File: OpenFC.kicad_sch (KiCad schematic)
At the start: 0 parts

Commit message: First routing
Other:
- sheet ELRS ports: added ESP8285_EN, ESP8285_RST; removed none
- sheet RP2350A ports: added ESP8285_EN, ESP8285_RST; removed none
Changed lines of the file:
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@@
+	(wire
+		(pts
+			(xy 87.63 76.2) (xy 104.14 76.2)
+		)
+		(stroke
+			(width 0)
+			(type default)
+		)
+	)
 	(wire
 		(pts
@@
 		(pts
 			(xy 87.63 97.79) (xy 104.14 97.79)
+		)
+		(stroke
+			(width 0)
+			(type default)
+		)
+	)
+	(wire
+		(pts
+			(xy 87.63 78.74) (xy 104.14 78.74)
 		)
 		(stroke
@@
 	)
 	(sheet
-		(at 64.77 80.01)
-		(size 22.86 7.62)
+		(at 64.77 72.39)
+		(size 22.86 15.24)
 		(exclude_from_sim no)
 		(in_bom yes)
@@
 		)
 		(property "Sheetname" "ELRS"
-			(at 64.77 79.2984 0)
+			(at 64.77 71.6784 0)
 			(effects
 				(font
@@
 		(pin "ELRX_TX" input
 			(at 87.63 85.09 0)
+			(effects
+				(font
+					(size 1.27 1.27)
+				)
+				(justify right)
+			)
+		)
+		(pin "ESP8285_EN" input
+			(at 87.63 78.74 0)
+			(effects
+				(font
+					(size 1.27 1.27)
+				)
+				(justify right)
+			)
+		)
+		(pin "ESP8285_RST" input
+			(at 87.63 76.2 0)
 			(effects
 				(font
@@
 			)
 		)
+		(pin "ESP8285_EN" input
+			(at 104.14 78.74 180)
+			(effects
+				(font
+					(size 1.27 1.27)
+				)
+				(justify left)
+			)
+		)
+		(pin "ESP8285_RST" input
+			(at 104.14 76.2 180)
+			(effects
+				(font
+					(size 1.27 1.27)
+				)
+				(justify left)
+			)
+		)

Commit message: almost finished routing
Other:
- sheet ELRS ports: added ESP_BOOT0; removed ESP8285_RST
- sheet RP2350A ports: added ESP_BOOT0; removed ESP8285_RST
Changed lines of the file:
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@@
 			)
 		)
-		(pin "ESP8285_RST" input
+		(pin "ESP_BOOT0" input
 			(at 87.63 76.2 0)
 			(effects
@@
 			)
 		)
-		(pin "ESP8285_RST" input
+		(pin "ESP_BOOT0" input
 			(at 104.14 76.2 180)
 			(effects

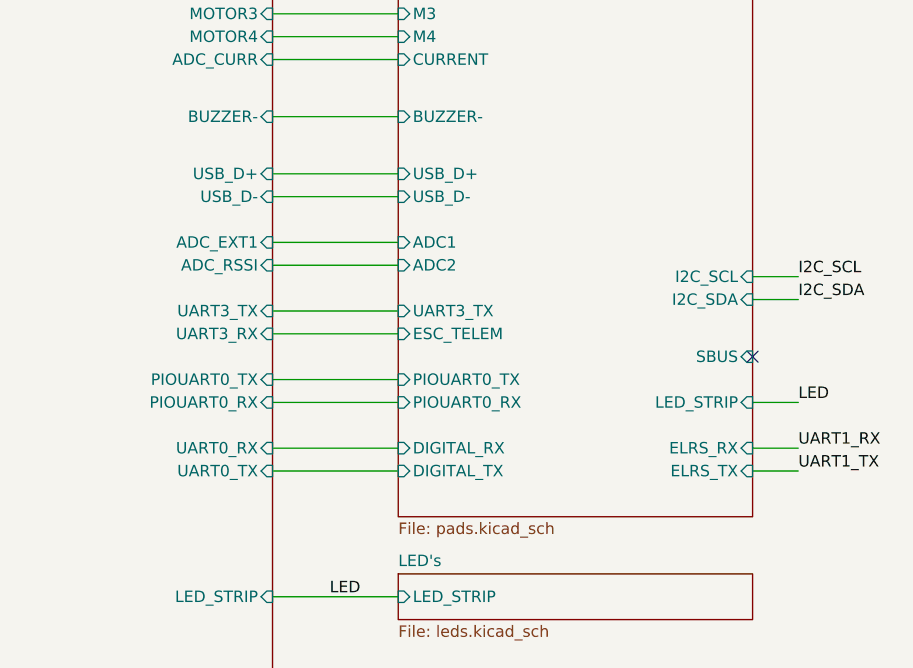
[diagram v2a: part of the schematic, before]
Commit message: Switched to RP2354A and re-routed
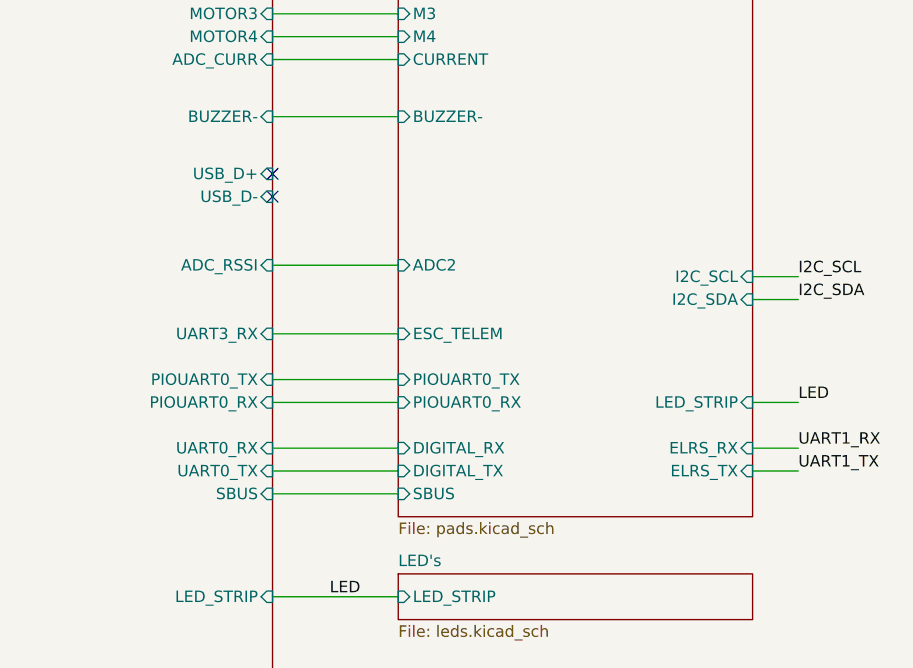
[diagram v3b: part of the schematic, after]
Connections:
- no-connect marks 1 -> 2
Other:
- sheet PADS ports: added none; removed ADC1, UART3_TX, USB_D+, USB_D-
- sheet RP2350A ports: added SBUS; removed ADC_EXT1, UART3_TX
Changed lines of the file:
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@@
 	)
 	(no_connect
-		(at 219.71 118.11)
+		(at 166.37 100.33)
+	)
+	(no_connect
+		(at 166.37 97.79)
 	)
 	(wire
@@
 		)
 	)
-	(wire
-		(pts
-			(xy 166.37 105.41) (xy 180.34 105.41)
-		)
-		(stroke
-			(width 0)
-			(type default)
-		)
-	)
 	(bus
 		(pts
@@
 		)
 	)
-	(wire
-		(pts
-			(xy 166.37 97.79) (xy 180.34 97.79)
-		)
-		(stroke
-			(width 0)
-			(type default)
-		)
-	)
 	(bus
 		(pts
@@
 	(wire
 		(pts
-			(xy 166.37 100.33) (xy 180.34 100.33)
-		)
-		(stroke
-			(width 0)
-			(type default)
-		)
-	)
-	(wire
-		(pts
-			(xy 166.37 113.03) (xy 180.34 113.03)
-		)
-		(stroke
-			(width 0)
-			(type default)
-		)
-	)
-	(wire
-		(pts
 			(xy 87.63 97.79) (xy 104.14 97.79)
 		)
@@
 		(pts
 			(xy 219.71 111.76) (xy 224.79 111.76)
+		)
+		(stroke
+			(width 0)
+			(type default)
+		)
+	)
+	(wire
+		(pts
+			(xy 166.37 133.35) (xy 180.34 133.35)
 		)
 		(stroke
@@
 			)
 		)
-		(pin "ADC_EXT1" input
-			(at 166.37 105.41 0)
-			(effects
-				(font
-					(size 1.27 1.27)
-				)
-				(justify right)
-			)
-		)
 		(pin "ADC_CURR" input
 			(at 166.37 85.09 0)
@@
 			)
 		)
-		(pin "UART3_TX" input
-			(at 166.37 113.03 0)
-			(effects
-				(font
-					(size 1.27 1.27)
-				)
-				(justify right)
-			)
-		)
 		(pin "MOTOR1" input
 			(at 166.37 74.93 0)
@@
 				)
 				(justify left)
+			)
+		)
+		(pin "SBUS" input
+			(at 166.37 133.35 0)
+			(effects
+				(font
+					(size 1.27 1.27)
+				)
+				(justify right)
 			)
 		)
@@
 		)
 		(pin "SBUS" input
-			(at 219.71 118.11 0)
-			(effects
-				(font
-					(size 1.27 1.27)
-				)
-				(justify right)
-			)
-		)
-		(pin "USB_D+" input
-			(at 180.34 97.79 180)
-			(effects
-				(font
-					(size 1.27 1.27)
-				)
-				(justify left)
-			)
-		)
-		(pin "USB_D-" input
-			(at 180.34 100.33 180)
+			(at 180.34 133.35 180)
 			(effects
 				(font
@@
 			)
 		)
-		(pin "ADC1" input
-			(at 180.34 105.41 180)
-			(effects
-				(font
-					(size 1.27 1.27)
-				)
-				(justify left)
-			)
-		)
 		(pin "ADC2" input
 			(at 180.34 107.95 180)
 			(effects
 				(font
-					(size 1.27 1.27)
-				)
-				(justify left)
-			)
-		)
-		(pin "UART3_TX" input
-			(at 180.34 113.03 180)
-			(effects
-				(font

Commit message: Added Open-OSD-X and new layout
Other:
- sheet OSD: file untitled.kicad_sch -> osd.kicad_sch
- sheet OSD ports: added OSD_RX, OSD_TX, SA_OUT, VIDEO_IN, VIDEO_OUT; removed none
- sheet PADS ports: added CAMERA, SMARTAUDIO, VTX; removed none
- sheet RP2350A ports: added UART2_RX, UART2_TX; removed none
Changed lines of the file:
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@@
+		)
+	)
+	(wire
+		(pts
+			(xy 162.56 54.61) (xy 193.04 54.61)
+		)
+		(stroke
+			(width 0)
+			(type default)
 		)
 	)
@@
 	(wire
 		(pts
+			(xy 146.05 64.77) (xy 146.05 68.58)
+		)
+		(stroke
+			(width 0)
+			(type default)
+		)
+	)
+	(wire
+		(pts
 			(xy 166.37 123.19) (xy 180.34 123.19)
 		)
@@
 	(wire
 		(pts
+			(xy 148.59 64.77) (xy 148.59 68.58)
+		)
+		(stroke
+			(width 0)
+			(type default)
+		)
+	)
+	(wire
+		(pts
 			(xy 166.37 91.44) (xy 180.34 91.44)
 		)
@@
 	(wire
 		(pts
+			(xy 193.04 54.61) (xy 193.04 69.85)
+		)
+		(stroke
+			(width 0)
+			(type default)
+		)
+	)
+	(wire
+		(pts
+			(xy 162.56 52.07) (xy 195.58 52.07)
+		)
+		(stroke
+			(width 0)
+			(type default)
+		)
+	)
+	(wire
+		(pts
 			(xy 166.37 115.57) (xy 180.34 115.57)
 		)
@@
 	(wire
 		(pts
+			(xy 198.12 49.53) (xy 162.56 49.53)
+		)
+		(stroke
+			(width 0)
+			(type default)
+		)
+	)
+	(wire
+		(pts
+			(xy 198.12 69.85) (xy 198.12 49.53)
+		)
+		(stroke
+			(width 0)
+			(type default)
+		)
+	)
+	(wire
+		(pts
 			(xy 87.63 148.59) (xy 92.71 148.59)
 		)
@@
 		(pts
 			(xy 87.63 82.55) (xy 104.14 82.55)
+		)
+		(stroke
+			(width 0)
+			(type default)
+		)
+	)
+	(wire
+		(pts
+			(xy 195.58 52.07) (xy 195.58 69.85)
 		)
 		(stroke
@@
 	)
 	(sheet
-		(at 140.97 166.37)
-		(size 19.05 19.05)
+		(at 127 46.99)
+		(size 35.56 17.78)
 		(exclude_from_sim no)
 		(in_bom yes)
@@
 		)
 		(property "Sheetname" "OSD"
-			(at 140.97 165.6584 0)
+			(at 127 46.2784 0)
 			(effects
 				(font
@@
 			)
 		)
-		(property "Sheetfile" "untitled.kicad_sch"
-			(at 140.97 186.0046 0)
+		(property "Sheetfile" "osd.kicad_sch"
+			(at 127 65.3546 0)
 			(effects
 				(font
@@
 				)
 				(justify left top)
+			)
+		)
+		(pin "OSD_RX" input
+			(at 146.05 64.77 270)
+			(effects
+				(font
+					(size 1.27 1.27)
+				)
+				(justify left)
+			)
+		)
+		(pin "OSD_TX" input
+			(at 148.59 64.77 270)
+			(effects
+				(font
+					(size 1.27 1.27)
+				)
+				(justify left)
+			)
+		)
+		(pin "SA_OUT" input
+			(at 162.56 52.07 0)
+			(effects
+				(font
+					(size 1.27 1.27)
+				)
+				(justify right)
+			)
+		)
+		(pin "VIDEO_IN" input
+			(at 162.56 49.53 0)
+			(effects
+				(font
+					(size 1.27 1.27)
+				)
+				(justify right)
+			)
+		)
+		(pin "VIDEO_OUT" input
+			(at 162.56 54.61 0)
+			(effects
+				(font
+					(size 1.27 1.27)
+				)
+				(justify right)
 			)
 		)
@@
 			)
 		)
+		(pin "UART2_RX" input
+			(at 148.59 68.58 90)
+			(effects
+				(font
+					(size 1.27 1.27)
+				)
+				(justify right)
+			)
+		)
+		(pin "UART2_TX" input
+			(at 146.05 68.58 90)
+			(effects
+				(font
+					(size 1.27 1.27)
+				)
+				(justify right)
+			)
+		)
 		(instances
 			(project "OpenFC"
@@
 			)
 		)
+		(pin "CAMERA" input
+			(at 198.12 69.85 90)
+			(effects
+				(font
+					(size 1.27 1.27)
+				)
+				(justify right)
+			)
+		)
+		(pin "SMARTAUDIO" input
+			(at 195.58 69.85 90)
+			(effects
+				(font
+					(size 1.27 1.27)
+				)
+				(justify right)
+			)
+		)
+		(pin "VTX" input
+			(at 193.04 69.85 90)
+			(effects
+				(font
+					(size 1.27 1.27)
+				)
+				(justify right)
+			)
+		)
 		(instances
 			(project "OpenFC"
@@
 	)
 	(sheet
-		(at 64.77 43.18)
-		(size 154.94 12.7)
+		(at 33.02 66.04)
+		(size 26.67 90.17)
 		(exclude_from_sim no)
 		(in_bom yes)
@@
 		)
 		(property "Sheetname" "POWER"
-			(at 64.77 42.4684 0)
+			(at 33.02 65.3284 0)
 			(effects
 				(font
@@
 		)
 		(property "Sheetfile" "power.kicad_sch"
-			(at 64.77 56.4646 0)
-			(effects
-				(font
+			(at 33.02 156.7946 0)
+			(effects
+				(font

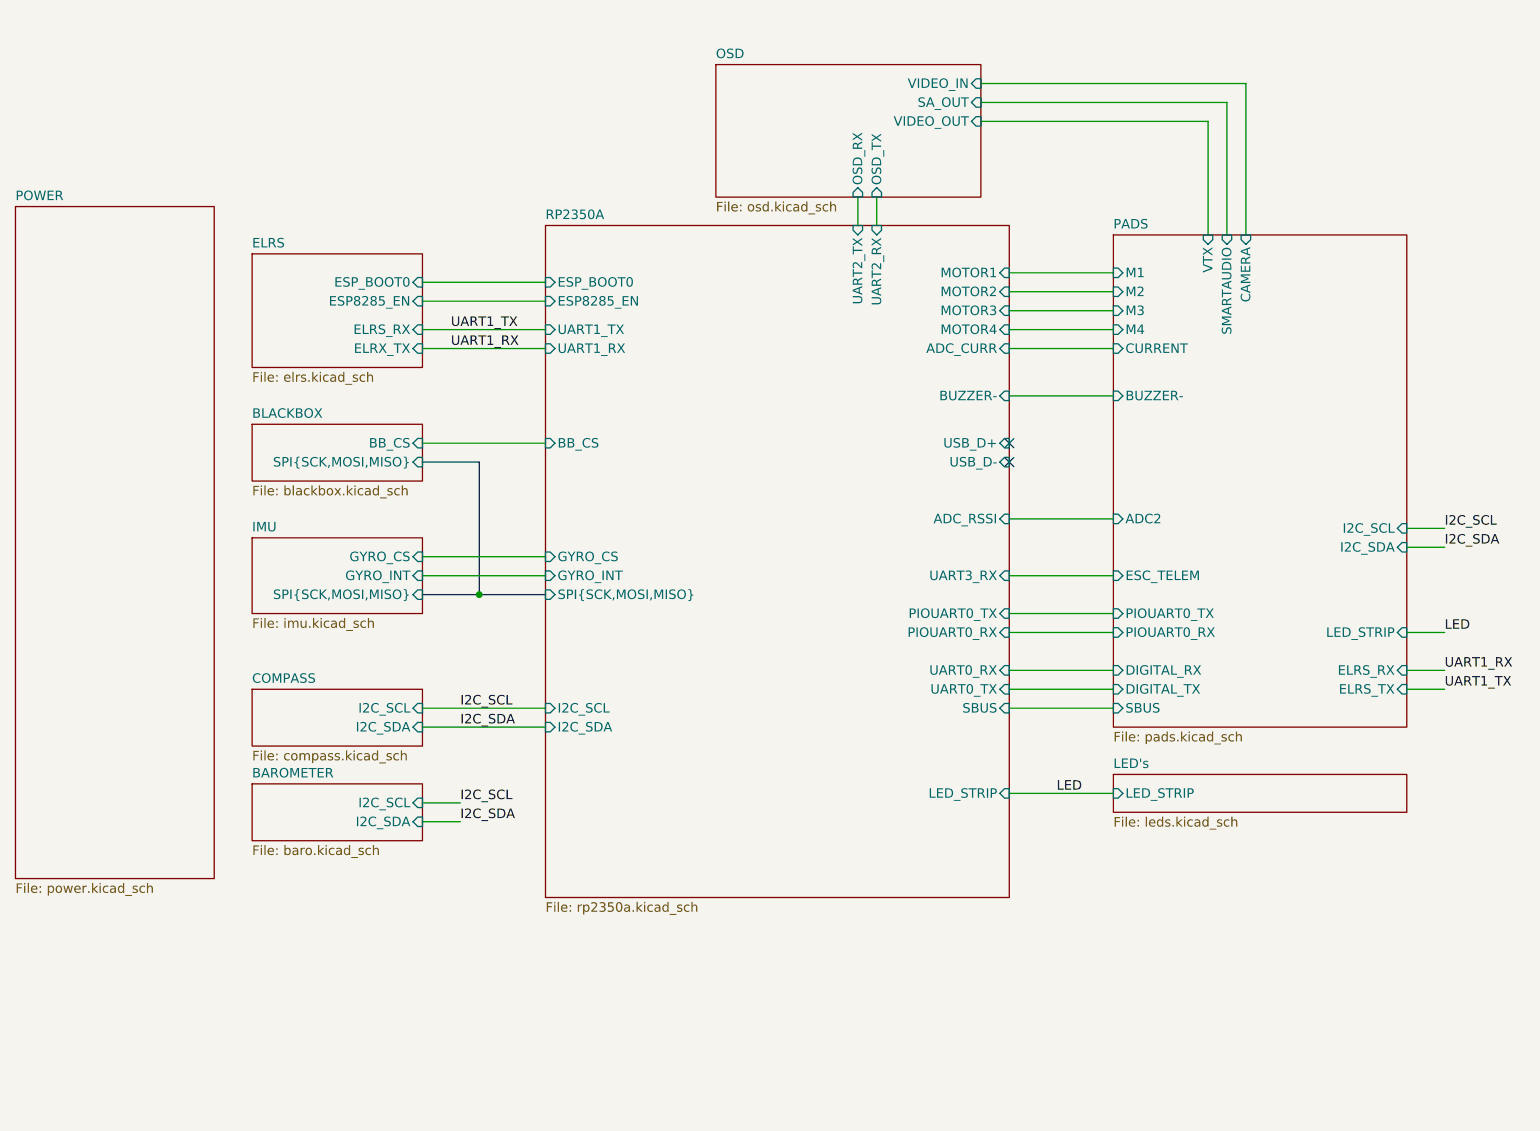
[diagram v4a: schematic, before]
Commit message: Switched to RP2354B for V2 of the FC for more IO. I want to try implement OSD on PIO state machine. I know BF already uses all of them but it should be possible and then later try to combine it witht the WS2812 protocol PIO2. If anybody here has any experience with analog OSD generation let me know, I just want to make a circuit that would allow further software development later. The reason I want to do it this way is it's cheap BOM<1 euro and low footprint, just 2 2x2 IC's and some passives.
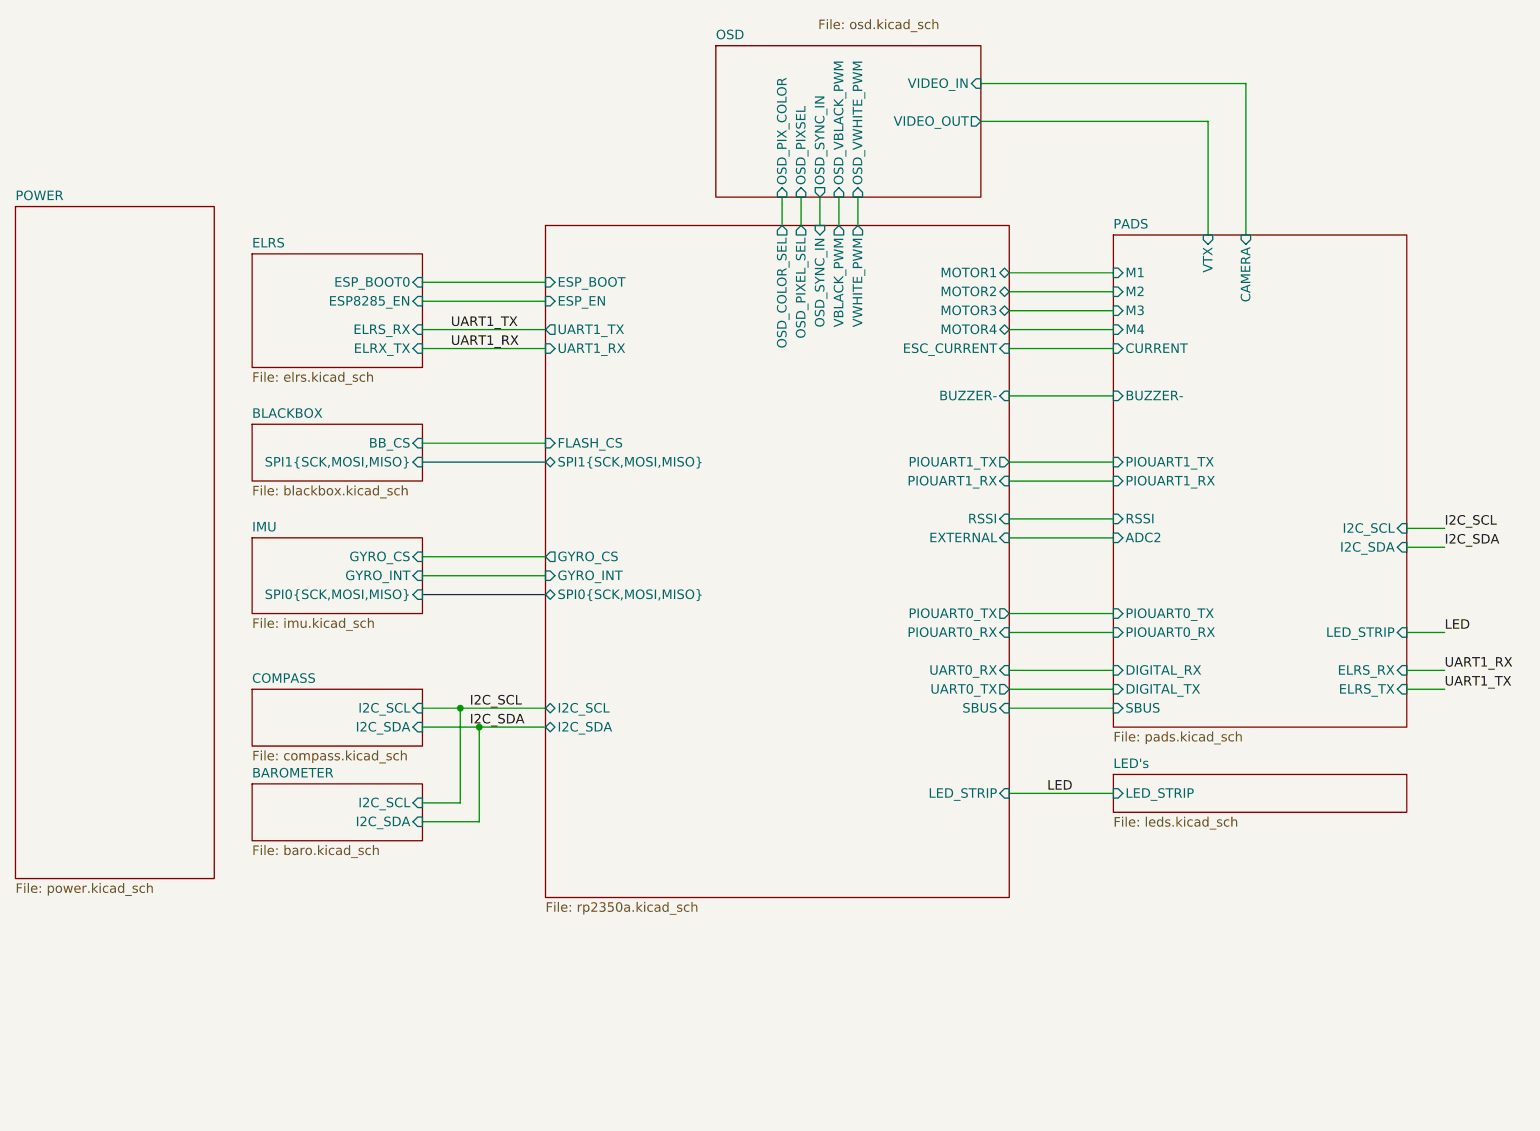
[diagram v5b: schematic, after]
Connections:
- no-connect marks 2 -> 0
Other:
- sheet BLACKBOX ports: added SPI1{SCK,MOSI,MISO}; removed SPI{SCK,MOSI,MISO}
- sheet IMU ports: added SPI0{SCK,MOSI,MISO}; removed SPI{SCK,MOSI,MISO}
- sheet OSD ports: added OSD_PIXSEL, OSD_PIX_COLOR, OSD_SYNC_IN, OSD_VBLACK_PWM, OSD_VWHITE_PWM; removed OSD_RX, OSD_TX, SA_OUT
- sheet PADS ports: added PIOUART1_RX, PIOUART1_TX, RSSI; removed ESC_TELEM, SMARTAUDIO
- sheet RP2350A ports: added ESC_CURRENT, ESP_BOOT, ESP_EN, EXTERNAL, FLASH_CS, OSD_COLOR_SEL, OSD_PIXEL_SEL, OSD_SYNC_IN, PIOUART1_RX, PIOUART1_TX, RSSI, SPI0{SCK,MOSI,MISO}, SPI1{SCK,MOSI,MISO}, VBLACK_PWM, VWHITE_PWM; removed ADC_CURR, ADC_RSSI, BB_CS, ESP8285_EN, ESP_BOOT0, SPI{SCK,MOSI,MISO}, UART2_RX, UART2_TX, UART3_RX, USB_D+, USB_D-
